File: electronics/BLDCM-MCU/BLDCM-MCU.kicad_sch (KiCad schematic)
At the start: 85 parts, among them J1 52991-0308, K1 EVPAKE31A, U1 STM32F446RE, U10 SK6805, U11 SK6805, U12 SK6805, U13 SK6805, U14 SK6805, U15 SK6805, U16 SK6805, U17 SK6805, U18 SK6805, U19 SK6805, U2 SN74LV1T34DBVR, U20 MT6701, U3 ISM330DHCX, U4 SK6805, U5 SK6805, U6 SK6805, U7 SK6805, U8 SK6805, U9 SK6805, Y1 ECS-3225MVLC-240-CN

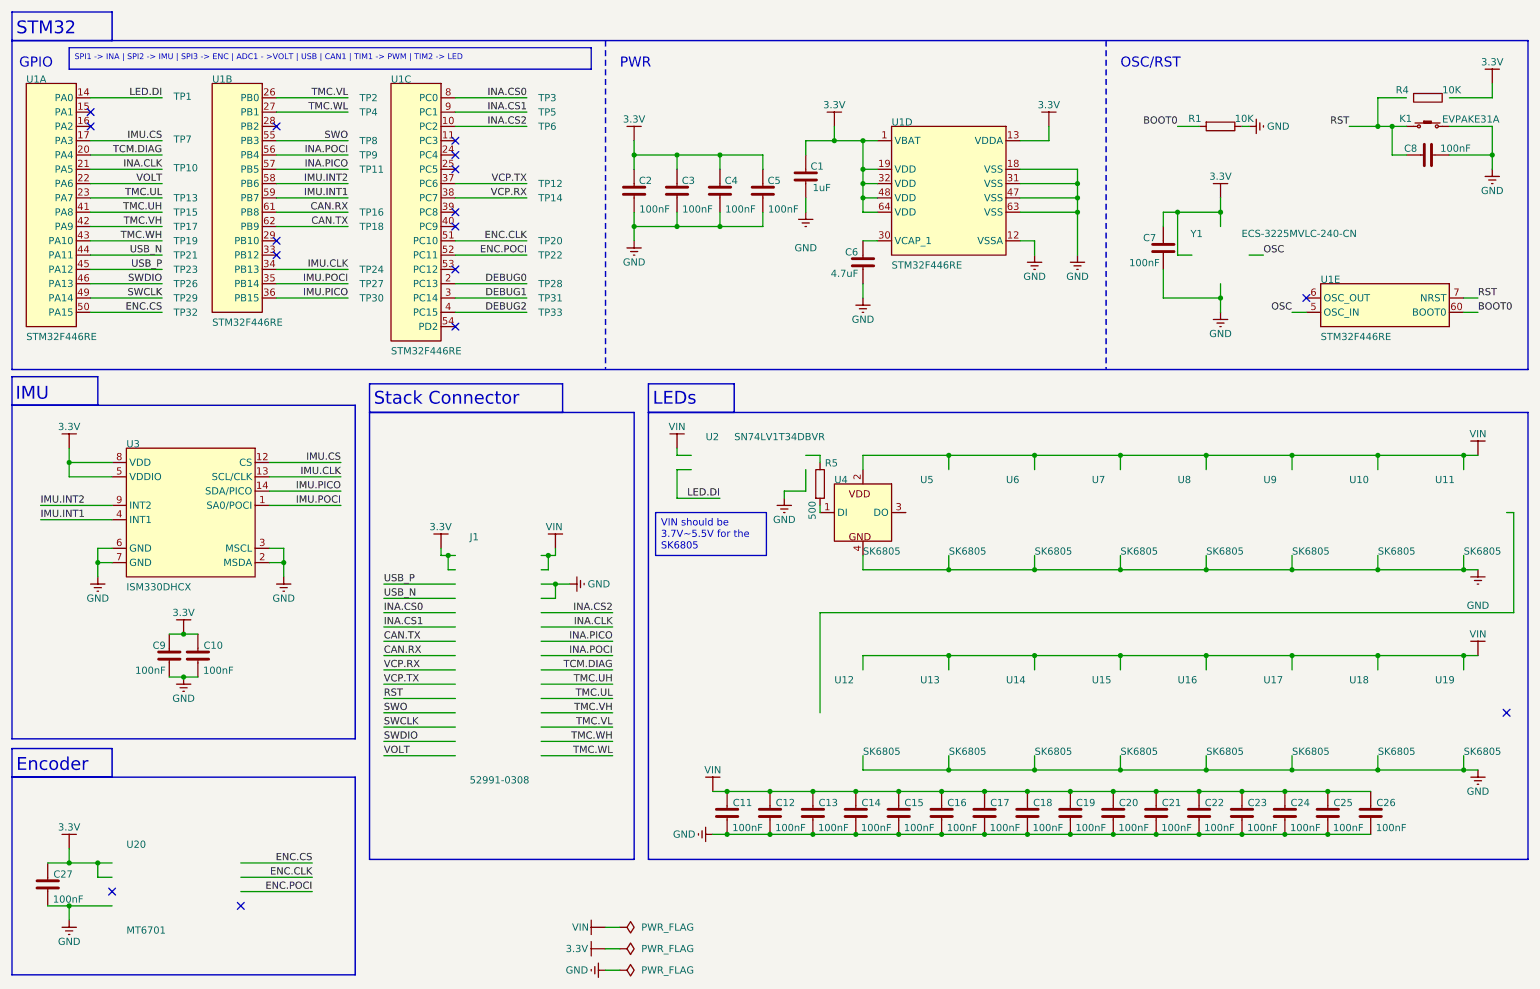
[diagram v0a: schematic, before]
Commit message: Refactor(pcb): Rename VIN to 5V in MCU PCB
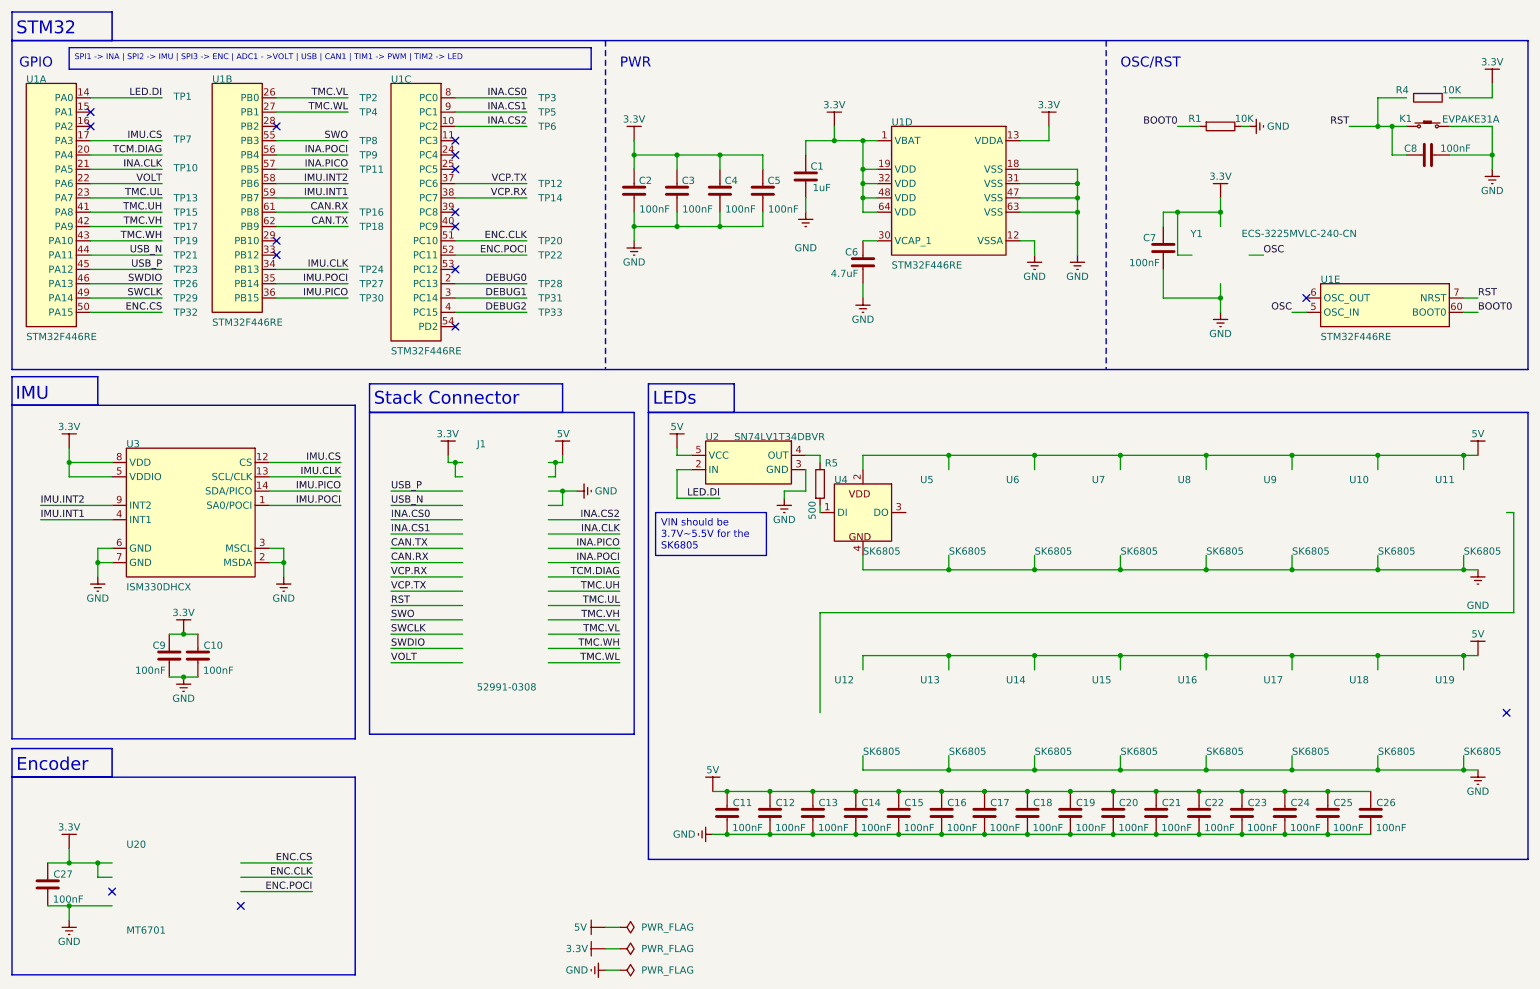
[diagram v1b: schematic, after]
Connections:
- net GND: now also U2.3 (GND)
- net LED.DI: now also U2.2 (IN)
- net at R5.2: now also U2.4 (OUT)
- net VIN renamed 5V
- net 5V: now also U2.5 (VCC)

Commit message: Feat(schematic): Use STM32 ADCs for phases curr/volt
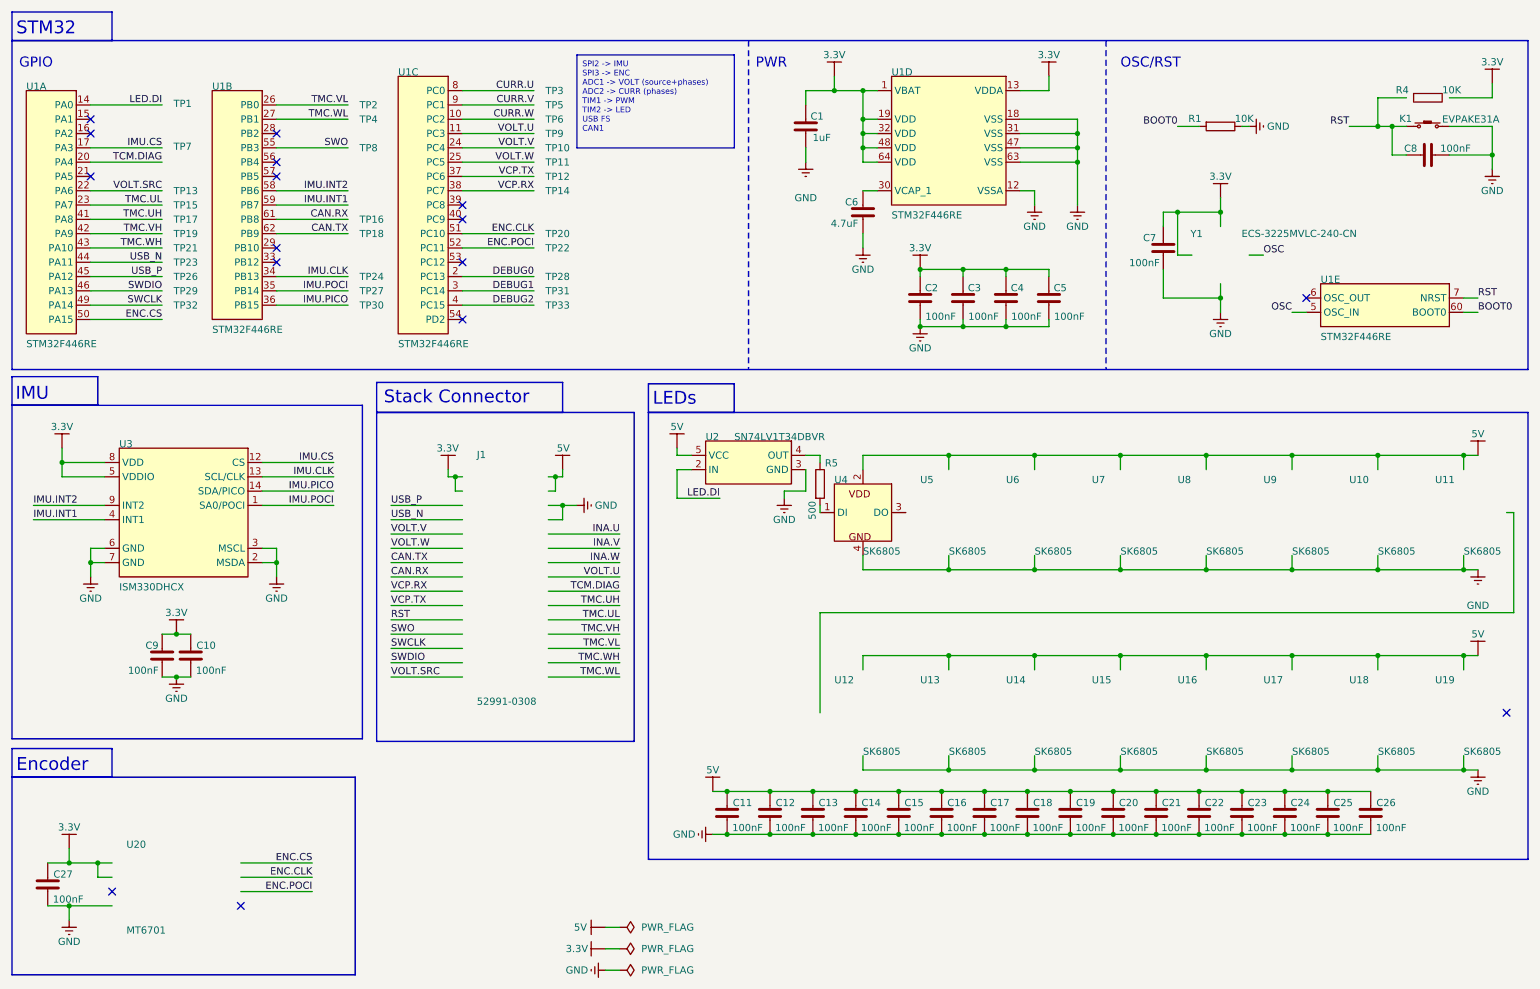
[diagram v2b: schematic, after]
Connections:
- net VOLT.U: now reaches U1.11 (PC3)
- net VOLT.V: now reaches U1.24 (PC4)
- net VOLT.W: now reaches U1.25 (PC5)
- net INA.CLK: no longer names the net of U1.21 (PA5)
- net INA.CS0 renamed CURR.U
- net INA.CS1 renamed CURR.V
- net INA.CS2 renamed CURR.W
- net INA.PICO: no longer names the net of U1.57 (PB5)
- net INA.POCI: no longer names the net of U1.56 (PB4)
- net VOLT renamed VOLT.SRC
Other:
- moved on the sheet: C1, C10, C2, C3, C4, C5, C6, C9, U1A, U1B, U1C, U1D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

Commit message: Feat(pcb): Route current sense
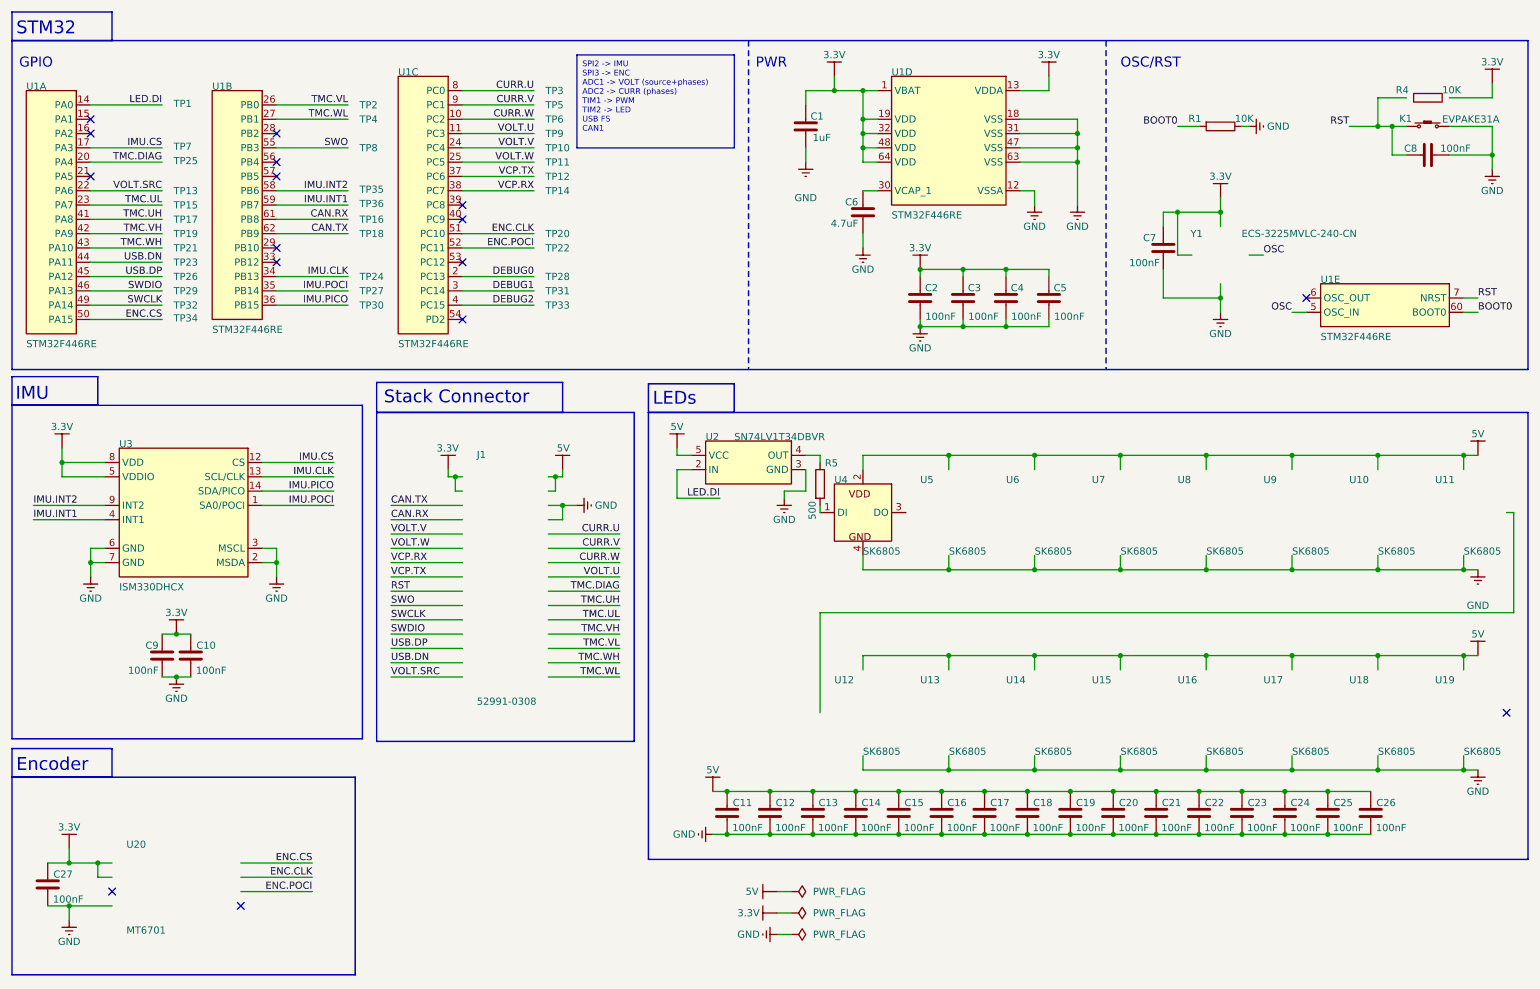
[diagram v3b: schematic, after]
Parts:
- added TP25, TP34, TP35, TP36: Test point 0.5mm, BrenoCQ:TP_0.5mm, symbol BrenoCQ:TP
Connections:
- net TCM.DIAG renamed TMC.DIAG
- net USB_N renamed USB.DN
- net USB_P renamed USB.DP

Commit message: Feat: v1.0 MCU/Power PCBs ready
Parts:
- removed U20: MT6701, BrenoCQ:SOP-8, symbol BrenoCQ:MT6701
- added C28: 10uF, BrenoCQ:C_0805, symbol BrenoCQ:C
- added TP37: Test point 0.5mm, BrenoCQ:TP_0.5mm, symbol BrenoCQ:TP
- added U20: AS5048A, BrenoCQ:TSSOP-14, symbol BrenoCQ:AS5048A
- C1: footprint BrenoCQ:C_0603 -> BrenoCQ:C_0402
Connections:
- net 3.3V: now also C28.2, U20.11 (VDD5V), U20.12 (VDD3V)
- net ENC.CLK: now also U20.2 (CLK)
- net ENC.CS: now also U20.1 (CS)
- net ENC.POCI: now also U20.3 (MISO)
- net GND: now also C28.1, U20.13 (GND)
- net ENC.PICO: now reaches U1.53 (PC12)
- net ENC.PICO: now also U20.4 (MOSI)
- no-connect marks 16 -> 14
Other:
- moved on the sheet: C27

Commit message: Feat: Add schematic PDFs for v1.0 PCBs
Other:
- company: (none) -> Breno Cunha Queiroz
- title: BLDCM - MCU -> BLDCM MCU
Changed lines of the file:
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@@
 	(paper "A4")
 	(title_block
-		(title "BLDCM - MCU")
-		(date "2025-05-06")
-		(rev "v3")
+		(title "BLDCM MCU")
+		(date "2025-07-19")
+		(rev "v1.0")
+		(company "Breno Cunha Queiroz")
 	)
 	(rectangle

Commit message: Feat: Setup KiCad project specific libraries
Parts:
- C6: footprint BrenoCQ:C_0603 -> BrenoCQ:C_0402
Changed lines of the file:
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@@
 			)
 		)
-		(property "Footprint" "BrenoCQ:C_0603"
+		(property "Footprint" "BrenoCQ:C_0402"
 			(at 170.18 49.53 0)
 			(effects

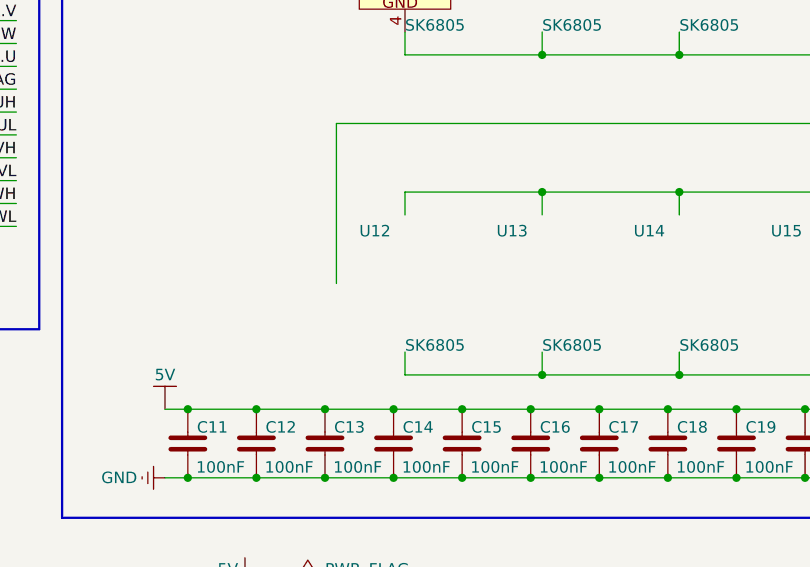
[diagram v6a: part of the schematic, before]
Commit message: Fix: PCB 3D model references
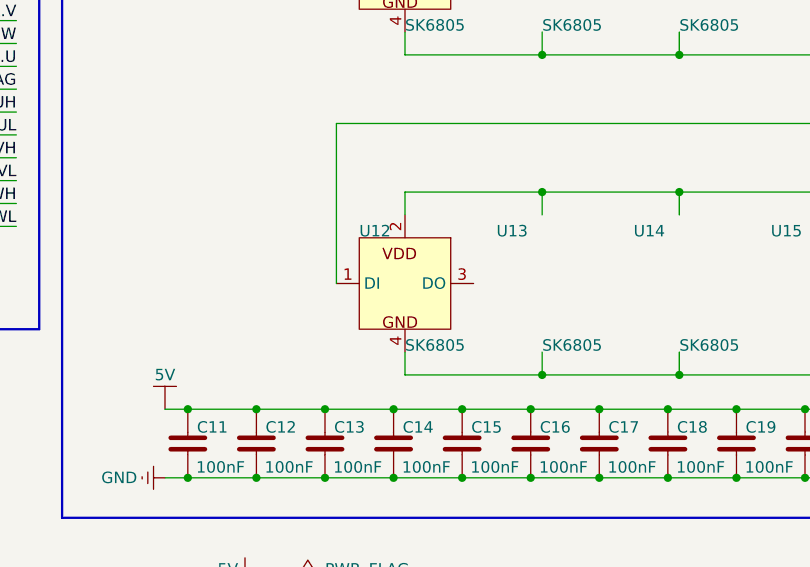
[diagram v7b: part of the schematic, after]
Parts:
- C6: footprint BrenoCQ:C_0402 -> BrenoCQ:C_0603
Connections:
- net 5V: now also U12.2 (VDD)
- net GND: now also U12.4 (GND)
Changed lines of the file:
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@@
 		(lib_id "BrenoCQ:LED_SK6805-EC15")
 		(at 165.1 140.97 0)
-		(unit 0)
+		(unit 1)
 		(exclude_from_sim no)
 		(in_bom yes)
@@
 				(path "/08ef0390-9acd-4f64-8b35-22fbbdf177e4"
 					(reference "U12")
-					(unit 0)
+					(unit 1)
 				)
 			)
@@
 			)
 		)
-		(property "Footprint" "BrenoCQ:C_0402"
+		(property "Footprint" "BrenoCQ:C_0603"
 			(at 170.18 49.53 0)
 			(effects
